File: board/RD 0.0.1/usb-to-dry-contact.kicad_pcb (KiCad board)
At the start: 2 copper layers, 28 parts, among them J1 480-37-1000, J2 CONN_OUT, J4 CONN_SWIM, K2 G5V-1, Q1 IRLML0030, U1 CP2102N-Axx-xQFN28, U2 STM8S003F3P

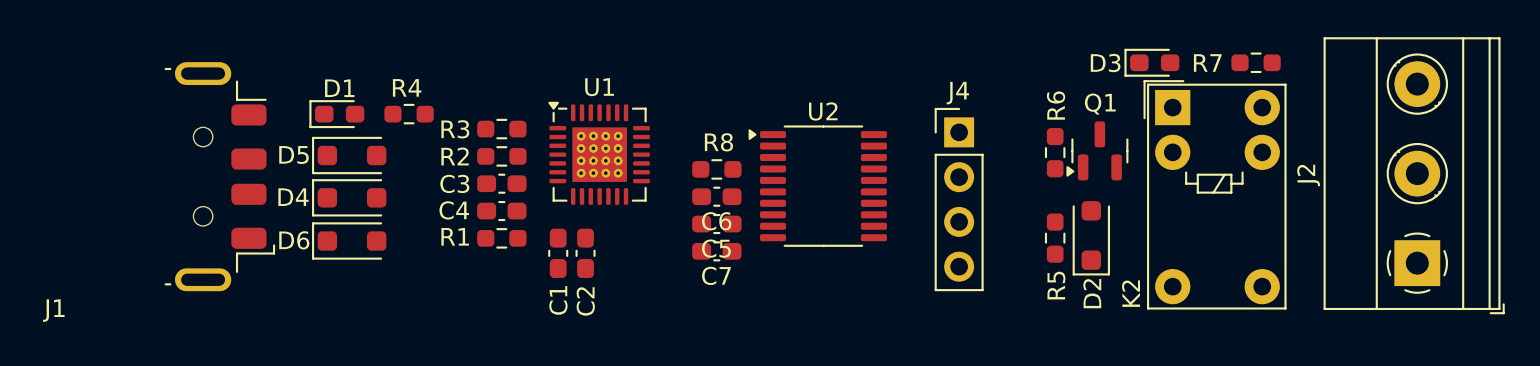
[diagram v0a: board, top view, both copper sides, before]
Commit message: Finish to route the board
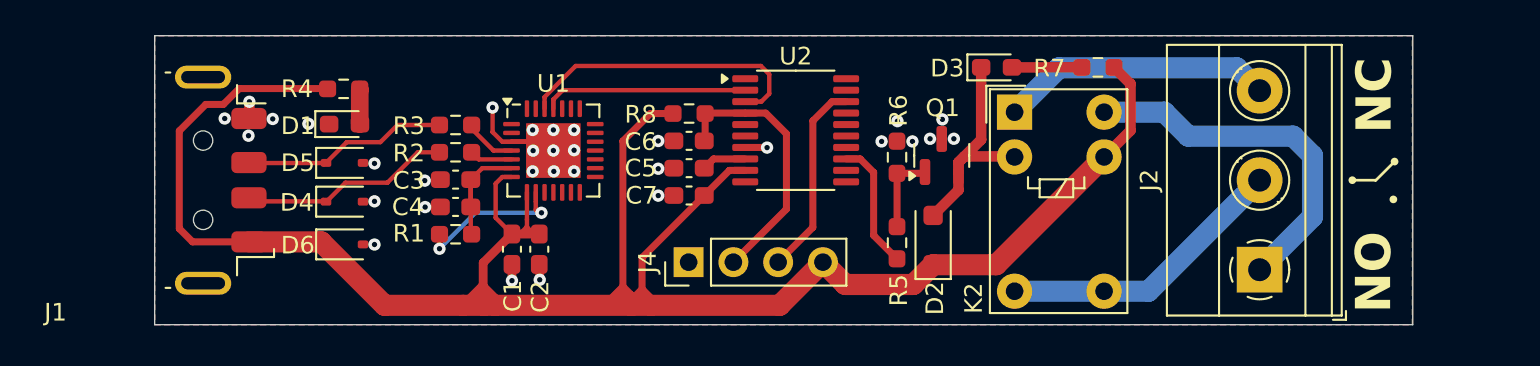
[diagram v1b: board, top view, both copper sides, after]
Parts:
- D4, D5, D6: footprint Diode_SMD:D_SOD-123F -> Diode_SMD:D_SOD-323
- U1: footprint Package_DFN_QFN:QFN-28-1EP_5x5mm_P0.5mm_EP3.1x3.1mm_ThermalVias -> Package_DFN_QFN:QFN-28-1EP_5x5mm_P0.5mm_EP3.1x3.1mm
- moved J4 17.0 mm to (149.4, 104.7), turned to 90 degrees
- moved D2 8.98 mm to (163.3, 103.4)
- moved D3 8.98 mm to (166.9, 93.6)
- moved K2 8.98 mm to (167.9, 96.1)
- moved Q1 8.98 mm to (163.8, 98.6)
- moved R5 8.98 mm to (161.3, 103.5)
- moved R6 8.98 mm to (161.3, 98.7)
- moved R7 8.98 mm to (172.7, 93.6)
- moved J2 8.96 mm to (181.8, 105.1)
- moved R4 3.98 mm to (129.9, 94.8), turned to 0 degrees
- moved C5 3.54 mm to (149.5, 99.3)
- moved C6 3.54 mm to (149.5, 97.8)
- moved R8 3.54 mm to (149.5, 96.2)
- moved C7 3.54 mm to (149.5, 100.9)
- moved U2 3.54 mm to (155.5, 97.2)
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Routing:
- net VBUS: track 0.00 -> 125.8 mm
- net RELAY_NO: track 0.00 -> 21.5 mm
- net USer_TX_uC_RX: track 0.00 -> 17.0 mm
- net RELAY_COM: track 0.00 -> 16.5 mm
- net RELAY_NC: track 0.00 -> 15.5 mm
- net RST: track 0.00 -> 15.2 mm
- net Net-(D2-A): track 0.00 -> 12.9 mm
- net D-: track 0.00 -> 12.4 mm
- net D+: track 0.00 -> 11.9 mm
- net USer_RX_uC_TX: track 0.00 -> 11.6 mm
- net SWIM: track 0.00 -> 11.2 mm
- net GND: track 0.00 -> 11.0 mm, vias 0 -> 32
- net Net-(U1-~{RST}): track 0.00 -> 8.85 mm, vias 0 -> 2
- net RELAY: track 0.00 -> 7.33 mm
- net VDD: track 0.00 -> 7.25 mm
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- added copper zone on B.Cu, net GND
- added copper zone on F.Cu, net GND
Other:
- board outline added: 71.4 x 16.4 mm
- rule pad_to_mask_clearance: 0 -> 0.038
- board text added: "NC"
- board text added: "NO"
- board text added: "USB to Dry Contact RD 0.0.1"

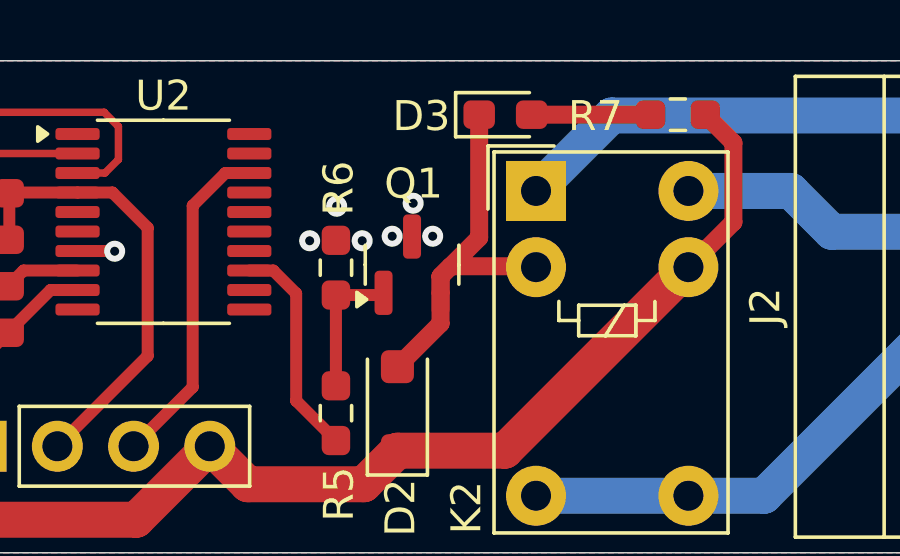
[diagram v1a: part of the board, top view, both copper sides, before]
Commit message: Change wrong symbol for the Relay MOSFET
The symbol has switched Drain pin and Source pin
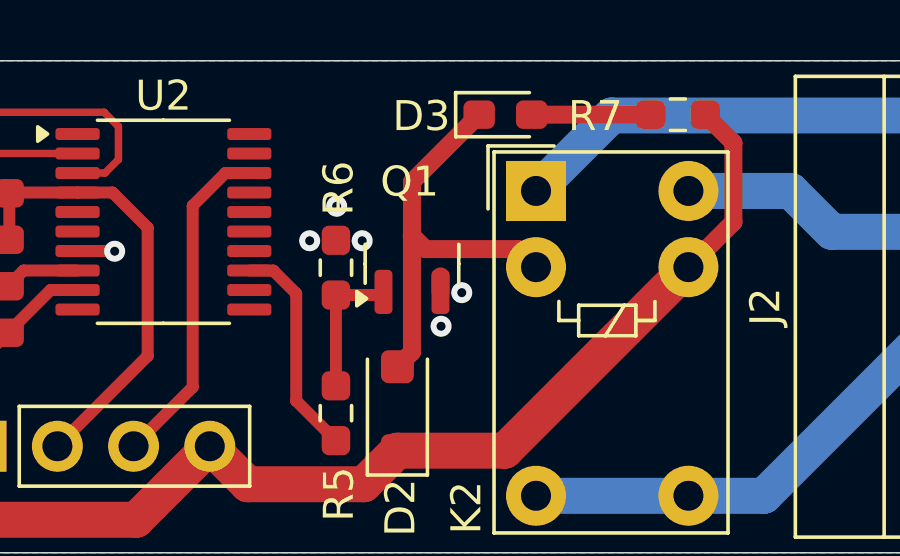
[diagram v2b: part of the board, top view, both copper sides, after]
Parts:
- D4, D5, D6: value D_Small -> BZT52B5V1S
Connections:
- Q1 pad 2: Net-(D2-A) -> GND
- Q1 pad 3: GND -> Net-(D2-A)
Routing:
- net Net-(D2-A): track 12.9 -> 14.1 mm
- net GND: track 11.0 -> 11.6 mm, vias 32 -> 31
